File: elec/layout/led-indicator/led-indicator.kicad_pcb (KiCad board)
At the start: 2 copper layers, 2 parts

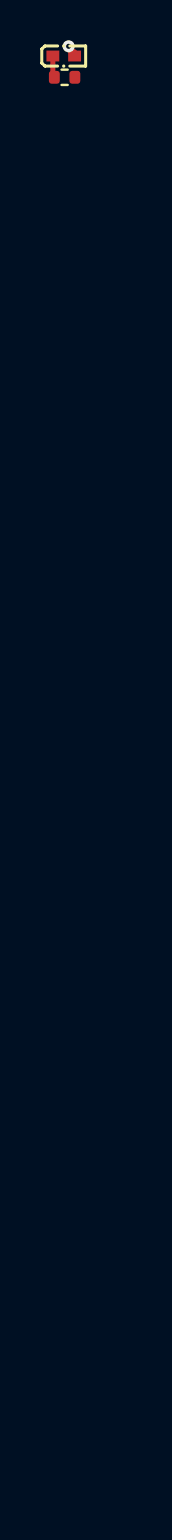
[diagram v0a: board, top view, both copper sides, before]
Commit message: rotat 90 degrees and move to kicad X0Y0
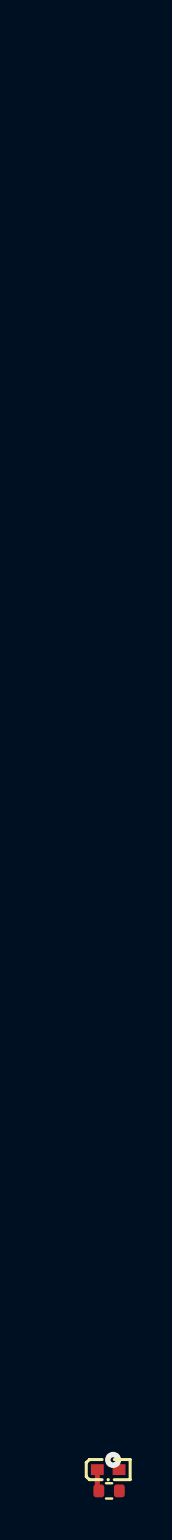
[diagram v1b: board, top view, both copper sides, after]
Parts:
- moved LED1 70.3 mm to (107.4, 158.8)
- moved R1 70.3 mm to (107.4, 159.9)
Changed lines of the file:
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@@
 	(footprint "lib:R0402"
 		(layer "F.Cu")
-		(at 105.209483 89.636524)
+		(at 107.419199 159.857306)
 		(descr "Resistor SMD 0402 (1005 Metric), square (rectangular) end terminal, IPC_7351 nominal, (Body size source: IPC-SM-782 page 72, https://www.pcb-3d.com/wordpress/wp-content/uploads/ipc-sm-782a_amendment_1_and_2.pdf), generated with kicad-footprint-generator")
 		(tags "resistor")
@@
 	(footprint "lib:LED0402-RD_ORANGE"
 		(layer "F.Cu")
-		(at 105.165 88.58)
+		(at 107.374716 158.800782)
 		(property "Reference" "LED1"
 			(at 0 -4 0)
@@
 	)
 	(segment
-		(start 104.625 88.58)
-		(end 104.625 89.76084)
+		(start 106.834716 159.981622)
+		(end 106.843878 159.990784)
 		(width 0.25)
+		(locked yes)
 		(layer "F.Cu")
 		(net 2)
 	)
 	(segment
-		(start 104.625 89.76084)
-		(end 104.634162 89.770002)
+		(start 106.834716 158.800782)
+		(end 106.834716 159.981622)
 		(width 0.25)
+		(locked yes)
 		(layer "F.Cu")
 		(net 2)
 	)
 	(segment
-		(start 105.705 88.392569)
-		(end 105.705 88.58)
+		(start 107.914716 158.613351)
+		(end 107.914716 158.800782)
 		(width 0.25)
+		(locked yes)
 		(layer "F.Cu")
 		(net 3)
 	)
-	(segment
-		(start 105.409468 88.097037)
-		(end 105.705 88.392569)
-		(width 0.25)
-		(layer "F.Cu")
-		(net 3)
-	)
 	(via
-		(at 105.409468 88.097037)
-		(size 0.6)
+		(at 107.619184 158.317819)
+		(size 0.8)
 		(drill 0.25)
 		(layers "F.Cu" "B.Cu")
+		(locked yes)
 		(net 3)
 	)
